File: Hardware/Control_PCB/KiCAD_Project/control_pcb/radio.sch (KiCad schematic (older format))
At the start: 15 parts, among them U2 SN74LVC1G18, U3 TX2M-400-5-NSSL, U8 MAX3232

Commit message: Draft of next layout
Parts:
- removed AE1: Antenna_Shield, lib_fp:SMA, symbol Device:Antenna_Shield
- removed C22, C23, C24, C25, C26, C8: 0.1u, Capacitors_SMD:C_0603_HandSoldering, symbol Device:C
- removed R22: 10k, Resistors_SMD:R_0603_HandSoldering, symbol Device:R
- removed R30: NP, Resistor_SMD:R_0603_1608Metric_Pad1.05x0.95mm_HandSolder, symbol Device:R
- removed U2: SN74LVC1G18, lib_fp:SN74LVC1G18DCKR, symbol lib_sch:SN74LVC1G18
- removed U3: TX2M-400-5-NSSL, lib_fp:TX2M, symbol lib_sch:TX2M-400-5-NSSL
- removed U8: MAX3232, Housings_SSOP:TSSOP-16_4.4x5mm_Pitch0.65mm, symbol Interface_UART:MAX3232
- added C6, C7, C8, C9: 1-0000007, capacitors_0603:1-0000007, symbol capacitors_0603:1-0000007
- added D4: Activity, LED_SMD:LED_0805_2012Metric, symbol Device:LED
- added D5: Error, LED_SMD:LED_0805_2012Metric, symbol Device:LED
- added J4: XBee ISP, Connector_PinHeader_2.54mm:PinHeader_2x04_P2.54mm_Vertical, symbol Connector_Generic:Conn_02x04_Odd_Even
- added J5: XBee_uC_ISP, Connector_PinHeader_2.54mm:PinHeader_2x03_P2.54mm_Vertical, symbol Connector_Generic:Conn_02x03_Odd_Even
- added R15, R16, R17: 10k, Resistor_SMD:R_0603_1608Metric, symbol Device:R
- added R19: 1-0000010, resistors_0603:1-0000010, symbol resistors_0603:1-0000010
- added R20, R21, R22: 1-0000006, resistors_0603:1-0000006, symbol resistors_0603:1-0000006
- added R24: 150, Resistor_SMD:R_0603_1608Metric, symbol Device:R
- added SW1: ID Select, lib_fp:KAE03TGGR, symbol Switch:SW_DIP_x03
- added U2: ATmega328P-AU, Package_QFP:TQFP-32_7x7mm_P0.8mm, symbol lib_sch:ATmega328P-AU
- added U3: XTend, lib_fp:XTend, symbol lib_sch:XTend
- added Y2: 16MHz, lib_fp:Resonator, symbol Device:Resonator_Small
- C10: renamed from C9; footprint Capacitors_SMD:C_0603_HandSoldering -> Capacitor_SMD:C_0603_1608Metric
- C11: renamed from C10; footprint Capacitors_SMD:C_0603_HandSoldering -> Capacitor_SMD:C_0603_1608Metric
- R23: value 10k -> 150; footprint Resistors_SMD:R_0603_HandSoldering -> Resistor_SMD:R_0603_1608Metric; Internal Part Number 1-0000010 -> 1-0000008
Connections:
- net labels added: 3V3_XBEE, RX_FROM_RADIO, RX_FROM_STM, TX_TO_RADIO, XBEE_uC_MISO, XBEE_uC_MOSI, XBEE_uC_RESET, XBEE_uC_SCK
- net labels removed: +BATT, Data_RS232, Programming_RS232, Radio_Serial_Select, TX_to_Radio
- wire segments 42 -> 96
- no-connect marks 6 -> 20
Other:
- note added: "The XBee controller recieves the serial stream from the STM32 of GPS and E-Field\ndata and retransmits it to the ground via XBee XTend in serial pass through mode.\nThe uC can perform downsampling or selective data transmission to reduce the\namount of data sent through the link, but currently we simply operate in a\npass through mode and it is there to allow for future expansion."
- note removed: "Populate for continous\ntransmission (test only)."
- moved on the sheet: C10, C11

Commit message: Add final production files
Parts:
- J4, J5: Internal Part Number (none) -> 0-0000000; Populated (none) -> 0
- U2: renamed from U3; Internal Part Number (none) -> 1-0000800; Populated (none) -> 1
- renumbered R19 to R16, R15 to R17, R16 to R18, R17 to R19, U2 to U3
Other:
- note added: "Jumper 1-2, 3-4 for normal\noperation, connect to 2, 4,\n6, 8 for XBee firmware updates\nand direct programming."
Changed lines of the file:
@@
 Sheet 2 6
 Title "Control Paddle Electronics - NSSL EFM"
-Date "2020-03-31"
-Rev "2.0"
+Date "2020-12-30"
+Rev "3.0"
 Comp "Leeman Geophysical LLC"
 Comment1 "(479) 373-3736"
@@
 Connection ~ 8775 3125
 $Comp
-L power:GND #PWR027
+L power:GND #PWR024
 U 1 1 5DEDBC1E
 P 8775 3175
-F 0 "#PWR027" H 8775 2925 50  0001 C CNN
+F 0 "#PWR024" H 8775 2925 50  0001 C CNN
 F 1 "GND" H 8625 3100 50  0000 C CNN
 F 2 "" H 8775 3175 50  0001 C CNN
@@
 $EndBitmap
 $Comp
-L lib_sch:XTend U3
+L lib_sch:XTend U2
 U 1 1 5FECB3EB
 P 9275 3775
-F 0 "U3" H 9725 4200 50  0000 C CNN
+F 0 "U2" H 9725 4200 50  0000 C CNN
 F 1 "XTend" H 9675 3200 50  0000 C CNN
 F 2 "lib_fp:XTend" H 9275 3775 50  0001 C CNN
 F 3 "" H 9275 3775 50  0001 C CNN
+F 4 "1-0000800" H 9275 3775 50  0001 C CNN "Internal Part Number"
+F 5 "1" H 9275 3775 50  0001 C CNN "Populated"
 	1    9275 3775
 	1    0    0    -1
@@
 NoConn ~ 9875 3925
 $Comp
-L power:GND #PWR030
+L power:GND #PWR028
 U 1 1 5FECEE80
 P 9275 4500
-F 0 "#PWR030" H 9275 4250 50  0001 C CNN
+F 0 "#PWR028" H 9275 4250 50  0001 C CNN
 F 1 "GND" H 9280 4327 50  0000 C CNN
 F 2 "" H 9275 4500 50  0001 C CNN
@@
 F 2 "Connector_PinHeader_2.54mm:PinHeader_2x04_P2.54mm_Vertical" H 7900 3725 50  0001 C CNN
 F 3 "~" H 7900 3725 50  0001 C CNN
+F 4 "0-0000000" H 7900 3725 50  0001 C CNN "Internal Part Number"
+F 5 "0" H 7900 3725 50  0001 C CNN "Populated"
 	1    7900 3725
 	1    0    0    -1
@@
 TX_TO_RADIO
 $Comp
-L lib_sch:ATmega328P-AU U2
+L lib_sch:ATmega328P-AU U3
 U 1 1 5FED41D3
 P 3375 3925
-F 0 "U2" H 3800 5375 50  0000 C CNN
+F 0 "U3" H 3800 5375 50  0000 C CNN
 F 1 "ATmega328P-AU" V 3375 3925 50  0000 C CNN
 F 2 "Package_QFP:TQFP-32_7x7mm_P0.8mm" H 3375 3925 50  0001 C CIN
@@
 	2775 3475 2775 3425
 $Comp
-L power:GND #PWR028
+L power:GND #PWR026
 U 1 1 5FED77F8
 P 2325 3425
-F 0 "#PWR028" H 2325 3175 50  0001 C CNN
+F 0 "#PWR026" H 2325 3175 50  0001 C CNN
 F 1 "GND" H 2330 3252 50  0000 C CNN
 F 2 "" H 2325 3425 50  0001 C CNN
@@
 NoConn ~ 3975 5125
 $Comp
-L power:GND #PWR032
+L power:GND #PWR030
 U 1 1 5FEE0BB1
 P 3375 5525
-F 0 "#PWR032" H 3375 5275 50  0001 C CNN
+F 0 "#PWR030" H 3375 5275 50  0001 C CNN
 F 1 "GND" H 3380 5352 50  0000 C CNN
 F 2 "" H 3375 5525 50  0001 C CNN
@@
 $EndComp
 $Comp
-L power:GND #PWR025
+L power:GND #PWR023
 U 1 1 5FEE3E70
 P 2475 2725
-F 0 "#PWR025" H 2475 2475 50  0001 C CNN
+F 0 "#PWR023" H 2475 2475 50  0001 C CNN
 F 1 "GND" H 2480 2552 50  0000 C CNN
 F 2 "" H 2475 2725 50  0001 C CNN
@@
 	2700 3000 1925 3000
 $Comp
-L resistors_0603:1-0000010 R19
+L resistors_0603:1-0000010 R16
 U 1 1 5FEE579A
 P 1925 2800
-F 0 "R19" V 2025 2750 50  0000 L CNN
+F 0 "R16" V 2025 2750 50  0000 L CNN
 F 1 "1-0000010" V 1925 2800 50  0001 C CNN
 F 2 "resistors_0603:1-0000010" V 1855 2800 50  0001 C CNN
@@
 	3375 1775 3375 1625
 $Comp
-L power:+3V3 #PWR022
+L power:+3V3 #PWR020
 U 1 1 5FEEF09F
 P 3375 1625
-F 0 "#PWR022" H 3375 1475 50  0001 C CNN
+F 0 "#PWR020" H 3375 1475 50  0001 C CNN
 F 1 "+3V3" H 3390 1798 50  0000 C CNN
 F 2 "" H 3375 1625 50  0001 C CNN
@@
 $EndComp
 $Comp
-L power:GND #PWR023
+L power:GND #PWR021
 U 1 1 5FEEF5CF
 P 2650 2275
-F 0 "#PWR023" H 2650 2025 50  0001 C CNN
+F 0 "#PWR021" H 2650 2025 50  0001 C CNN
 F 1 "GND" H 2500 2200 50  0000 C CNN
 F 2 "" H 2650 2275 50  0001 C CNN
@@
 	2650 2000 2650 1775
 $Comp
-L power:+3V3 #PWR024
+L power:+3V3 #PWR022
 U 1 1 5FEF3ED4
 P 1925 2650
-F 0 "#PWR024" H 1925 2500 50  0001 C CNN
+F 0 "#PWR022" H 1925 2500 50  0001 C CNN
 F 1 "+3V3" H 1940 2823 50  0000 C CNN
 F 2 "" H 1925 2650 50  0001 C CNN
@@
 Connection ~ 1925 3000
 $Comp
-L power:+3V3 #PWR033
+L power:+3V3 #PWR031
 U 1 1 5FEF71FA
 P 3700 6175
-F 0 "#PWR033" H 3700 6025 50  0001 C CNN
+F 0 "#PWR031" H 3700 6025 50  0001 C CNN
 F 1 "+3V3" H 3715 6348 50  0000 C CNN
 F 2 "" H 3700 6175 50  0001 C CNN
@@
 	3700 6275 4350 6275
 $Comp
-L power:GND #PWR034
+L power:GND #PWR032
 U 1 1 5FEFEED4
 P 3700 6375
-F 0 "#PWR034" H 3700 6125 50  0001 C CNN
+F 0 "#PWR032" H 3700 6125 50  0001 C CNN
 F 1 "GND" H 3705 6202 50  0000 C CNN
 F 2 "" H 3700 6375 50  0001 C CNN
@@
 AR Path="/5FFFBB18" Ref="#PWR?"  Part="1"
 AR Path="/5DEDFC42/5FFFBB18" Ref="#PWR?"  Part="1"
-AR Path="/5DED0CD0/5FFFBB18" Ref="#PWR031"  Part="1"
-F 0 "#PWR031" H 5250 5000 50  0001 C CNN
+AR Path="/5DED0CD0/5FFFBB18" Ref="#PWR029"  Part="1"
+F 0 "#PWR029" H 5250 5000 50  0001 C CNN
 F 1 "GND" H 5255 5077 50  0000 C CNN
 F 2 "" H 5250 5250 50  0001 C CNN
@@
 P 5350 3425
 AR Path="/5FEF08BD" Ref="R?"  Part="1"
-AR Path="/5DED0CD0/5FEF08BD" Ref="R17"  Part="1"
-F 0 "R17" V 5425 3375 50  0000 L CNN
+AR Path="/5DED0CD0/5FEF08BD" Ref="R19"  Part="1"
+F 0 "R19" V 5425 3375 50  0000 L CNN
 F 1 "10k" V 5350 3350 50  0000 L CNN
 F 2 "Resistor_SMD:R_0603_1608Metric" V 5280 3425 50  0001 C CNN
@@
 P 5200 3425
 AR Path="/5FEF08C5" Ref="R?"  Part="1"
-AR Path="/5DED0CD0/5FEF08C5" Ref="R16"  Part="1"
-F 0 "R16" V 5275 3375 50  0000 L CNN
+AR Path="/5DED0CD0/5FEF08C5" Ref="R18"  Part="1"
+F 0 "R18" V 5275 3375 50  0000 L CNN
 F 1 "10k" V 5200 3350 50  0000 L CNN
 F 2 "Resistor_SMD:R_0603_1608Metric" V 5130 3425 50  0001 C CNN
@@
 P 5050 3425
 AR Path="/5FEF08CD" Ref="R?"  Part="1"
-AR Path="/5DED0CD0/5FEF08CD" Ref="R15"  Part="1"
-F 0 "R15" V 5125 3375 50  0000 L CNN
+AR Path="/5DED0CD0/5FEF08CD" Ref="R17"  Part="1"
+F 0 "R17" V 5125 3375 50  0000 L CNN
 F 1 "10k" V 5050 3350 50  0000 L CNN
 F 2 "Resistor_SMD:R_0603_1608Metric" V 4980 3425 50  0001 C CNN
@@
 P 5200 3225
 AR Path="/5FEF08D9" Ref="#PWR?"  Part="1"
-AR Path="/5DED0CD0/5FEF08D9" Ref="#PWR016"  Part="1"
-F 0 "#PWR016" H 5200 3075 50  0001 C CNN
+AR Path="/5DED0CD0/5FEF08D9" Ref="#PWR025"  Part="1"
+F 0 "#PWR025" H 5200 3075 50  0001 C CNN
 F 1 "+3V3" H 5215 3398 50  0000 C CNN
 F 2 "" H 5200 3225 50  0001 C CNN
@@
 P 6075 3875
 AR Path="/5FEF08F1" Ref="#PWR?"  Part="1"
-AR Path="/5DED0CD0/5FEF08F1" Ref="#PWR017"  Part="1"
-F 0 "#PWR017" H 6075 3625 50  0001 C CNN
+AR Path="/5DED0CD0/5FEF08F1" Ref="#PWR027"  Part="1"
+F 0 "#PWR027" H 6075 3625 50  0001 C CNN
 F 1 "GND" H 6080 3702 50  0000 C CNN
 F 2 "" H 6075 3875 50  0001 C CNN
@@
 F 2 "Connector_PinHeader_2.54mm:PinHeader_2x03_P2.54mm_Vertical" H 3400 6275 50  0001 C CNN
 F 3 "~" H 3400 6275 50  0001 C CNN
+F 4 "0-0000000" H 3400 6275 50  0001 C CNN "Internal Part Number"
+F 5 "0" H 3400 6275 50  0001 C CNN "Populated"
 	1    3400 6275
 	1    0    0    -1
@@
 Text GLabel 9275 2825 1    50   UnSpc ~ 0
 3V3_XBEE
+Text Notes 7450 4375 0    50   ~ 0
+Jumper 1-2, 3-4 for normal\noperation, connect to 2, 4,\n6, 8 for XBee firmware updates\nand direct programming.
 $EndSCHEMATC

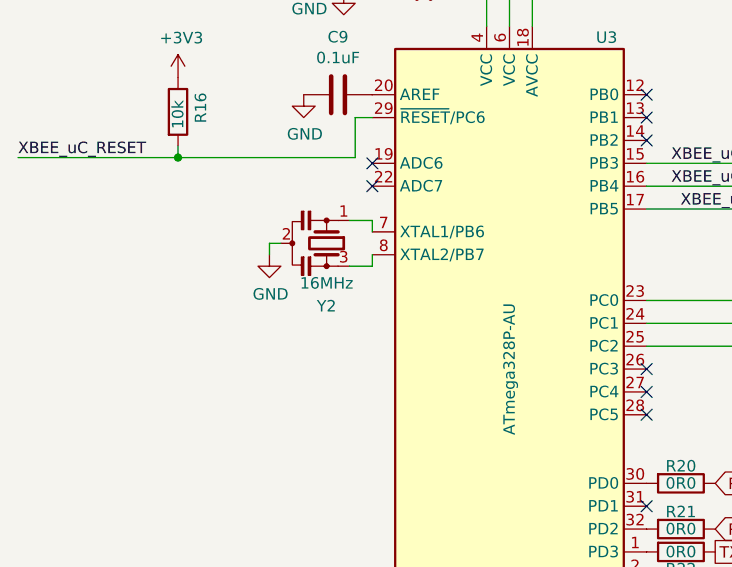
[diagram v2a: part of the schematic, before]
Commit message: Fix incorrect crystal part numbers and add production files for Rev 3.0
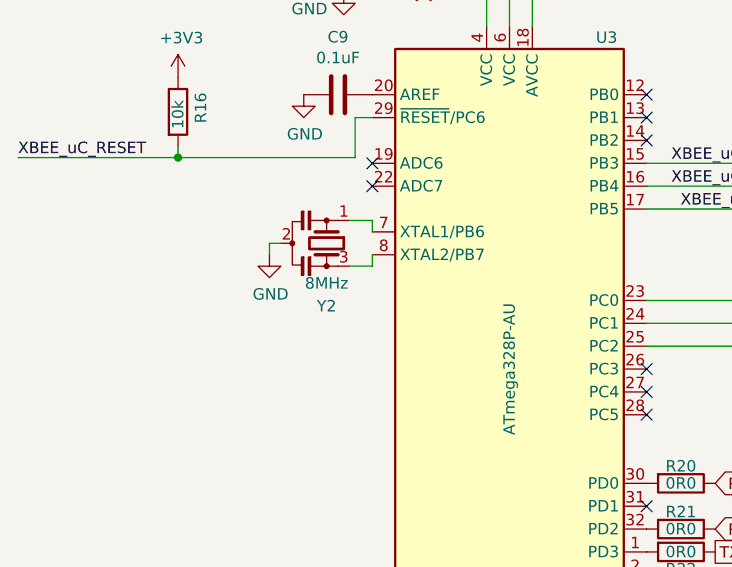
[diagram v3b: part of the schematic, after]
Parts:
- Y2: value 16MHz -> 8MHz; Internal Part Number 1-0000569 -> 1-0000721
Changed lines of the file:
@@
 P 2575 3375
 F 0 "Y2" V 2850 3375 50  0000 C CNN
-F 1 "16MHz" V 2750 3375 50  0000 C CNN
+F 1 "8MHz" V 2750 3375 50  0000 C CNN
 F 2 "lib_fp:Resonator" H 2550 3375 50  0001 C CNN
 F 3 "~" H 2550 3375 50  0001 C CNN
-F 4 "1-0000569" H 2575 3375 50  0001 C CNN "Internal Part Number"
+F 4 "1-0000721" H 2575 3375 50  0001 C CNN "Internal Part Number"
 F 5 "1" H 2575 3375 50  0001 C CNN "Populated"
 	1    2575 3375

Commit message: Control Rev 3.1
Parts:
- D4, D5: footprint LED_SMD:LED_0805_2012Metric -> LED_THT:LED_D3.0mm_Horizontal_O1.27mm_Z2.0mm_Clear
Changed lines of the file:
@@
 Sheet 2 6
 Title "Control Paddle Electronics - NSSL EFM"
-Date "2020-12-30"
-Rev "3.0"
+Date "2021-11-22"
+Rev "3.1"
 Comp "Leeman Geophysical LLC"
 Comment1 "(479) 373-3736"
@@
 F 0 "D4" H 5018 4670 50  0000 C CNN
 F 1 "Activity" H 5018 4761 50  0000 C CNN
-F 2 "LED_SMD:LED_0805_2012Metric" H 5025 4925 50  0001 C CNN
+F 2 "LED_THT:LED_D3.0mm_Horizontal_O1.27mm_Z2.0mm_Clear" H 5025 4925 50  0001 C CNN
 F 3 "~" H 5025 4925 50  0001 C CNN
 F 4 "1-0000599" H 5025 4925 50  0001 C CNN "Internal Part Number"
@@
 F 0 "D5" H 5025 5350 50  0000 C CNN
 F 1 "Error" H 5025 5250 50  0000 C CNN
-F 2 "LED_SMD:LED_0805_2012Metric" H 5025 5150 50  0001 C CNN
+F 2 "LED_THT:LED_D3.0mm_Horizontal_O1.27mm_Z2.0mm_Clear" H 5025 5150 50  0001 C CNN
 F 3 "~" H 5025 5150 50  0001 C CNN
 F 4 "1-0000600" H 5025 5150 50  0001 C CNN "Internal Part Number"
